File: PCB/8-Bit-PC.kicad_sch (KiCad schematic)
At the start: 0 parts

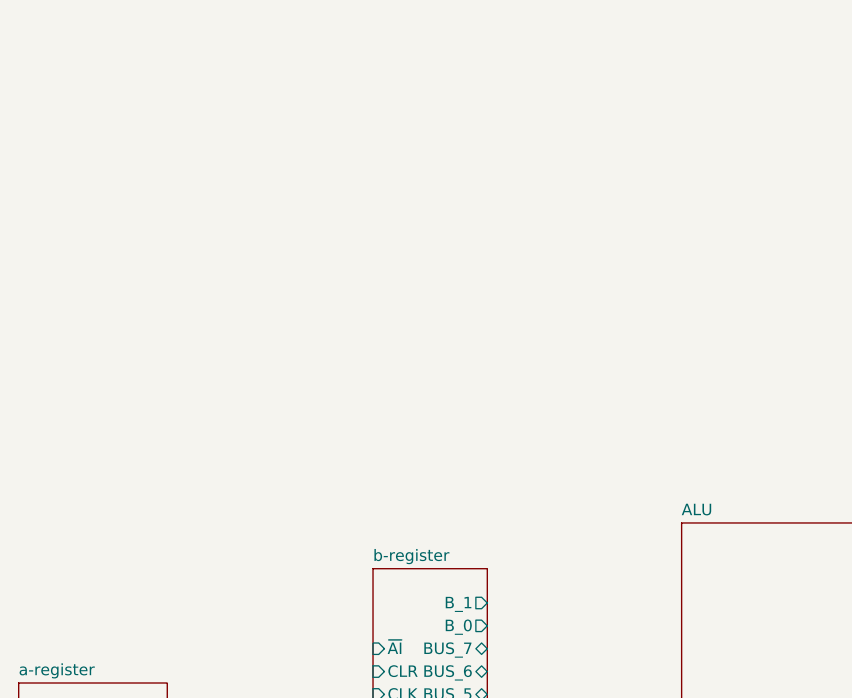
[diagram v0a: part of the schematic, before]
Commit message: got ready to add the cpu control and and out put modules
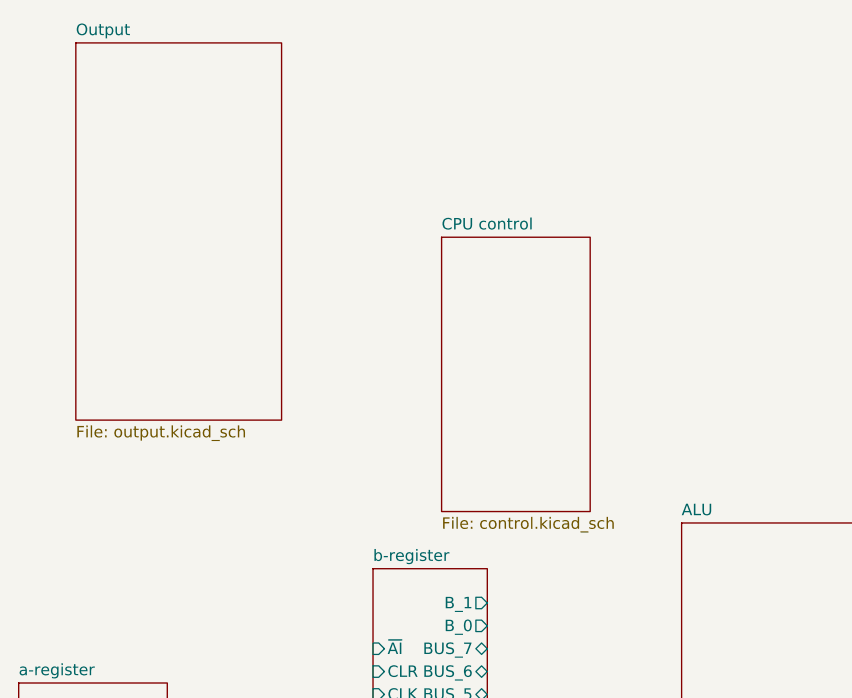
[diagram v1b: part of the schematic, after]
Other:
- added sheet CPU control (control.kicad_sch)
- added sheet Output (output.kicad_sch)
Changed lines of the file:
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@@
+	)
+	(sheet
+		(at 29.21 36.83)
+		(size 22.86 41.91)
+		(exclude_from_sim no)
+		(in_bom yes)
+		(on_board yes)
+		(dnp no)
+		(fields_autoplaced yes)
+		(stroke
+			(width 0.1524)
+			(type solid)
+		)
+		(fill
+			(color 0 0 0 0.0000)
+		)
+		(property "Sheetname" "Output"
+			(at 29.21 36.1184 0)
+			(effects
+				(font
+					(size 1.27 1.27)
+				)
+				(justify left bottom)
+			)
+		)
+		(property "Sheetfile" "output.kicad_sch"
+			(at 29.21 79.3246 0)
+			(effects
+				(font
+					(size 1.27 1.27)
+				)
+				(justify left top)
+			)
+		)
+		(instances
+			(project "8-Bit-PC"
+				(path "/48633dea-2de9-4b6f-aeff-2ee54233f918"
+					(page "9")
+				)
+			)
+		)
+	)
+	(sheet
+		(at 69.85 58.42)
+		(size 16.51 30.48)
+		(exclude_from_sim no)
+		(in_bom yes)
+		(on_board yes)
+		(dnp no)
+		(fields_autoplaced yes)
+		(stroke
+			(width 0.1524)
+			(type solid)
+		)
+		(fill
+			(color 0 0 0 0.0000)
+		)
+		(property "Sheetname" "CPU control"
+			(at 69.85 57.7084 0)
+			(effects
+				(font
+					(size 1.27 1.27)
+				)
+				(justify left bottom)
+			)
+		)
+		(property "Sheetfile" "control.kicad_sch"
+			(at 69.85 89.4846 0)
+			(effects
+				(font
+					(size 1.27 1.27)
+				)
+				(justify left top)
+			)
+		)
+		(instances
+			(project "8-Bit-PC"
+				(path "/48633dea-2de9-4b6f-aeff-2ee54233f918"
+					(page "10")
+				)
+			)
+		)
 	)
 	(sheet

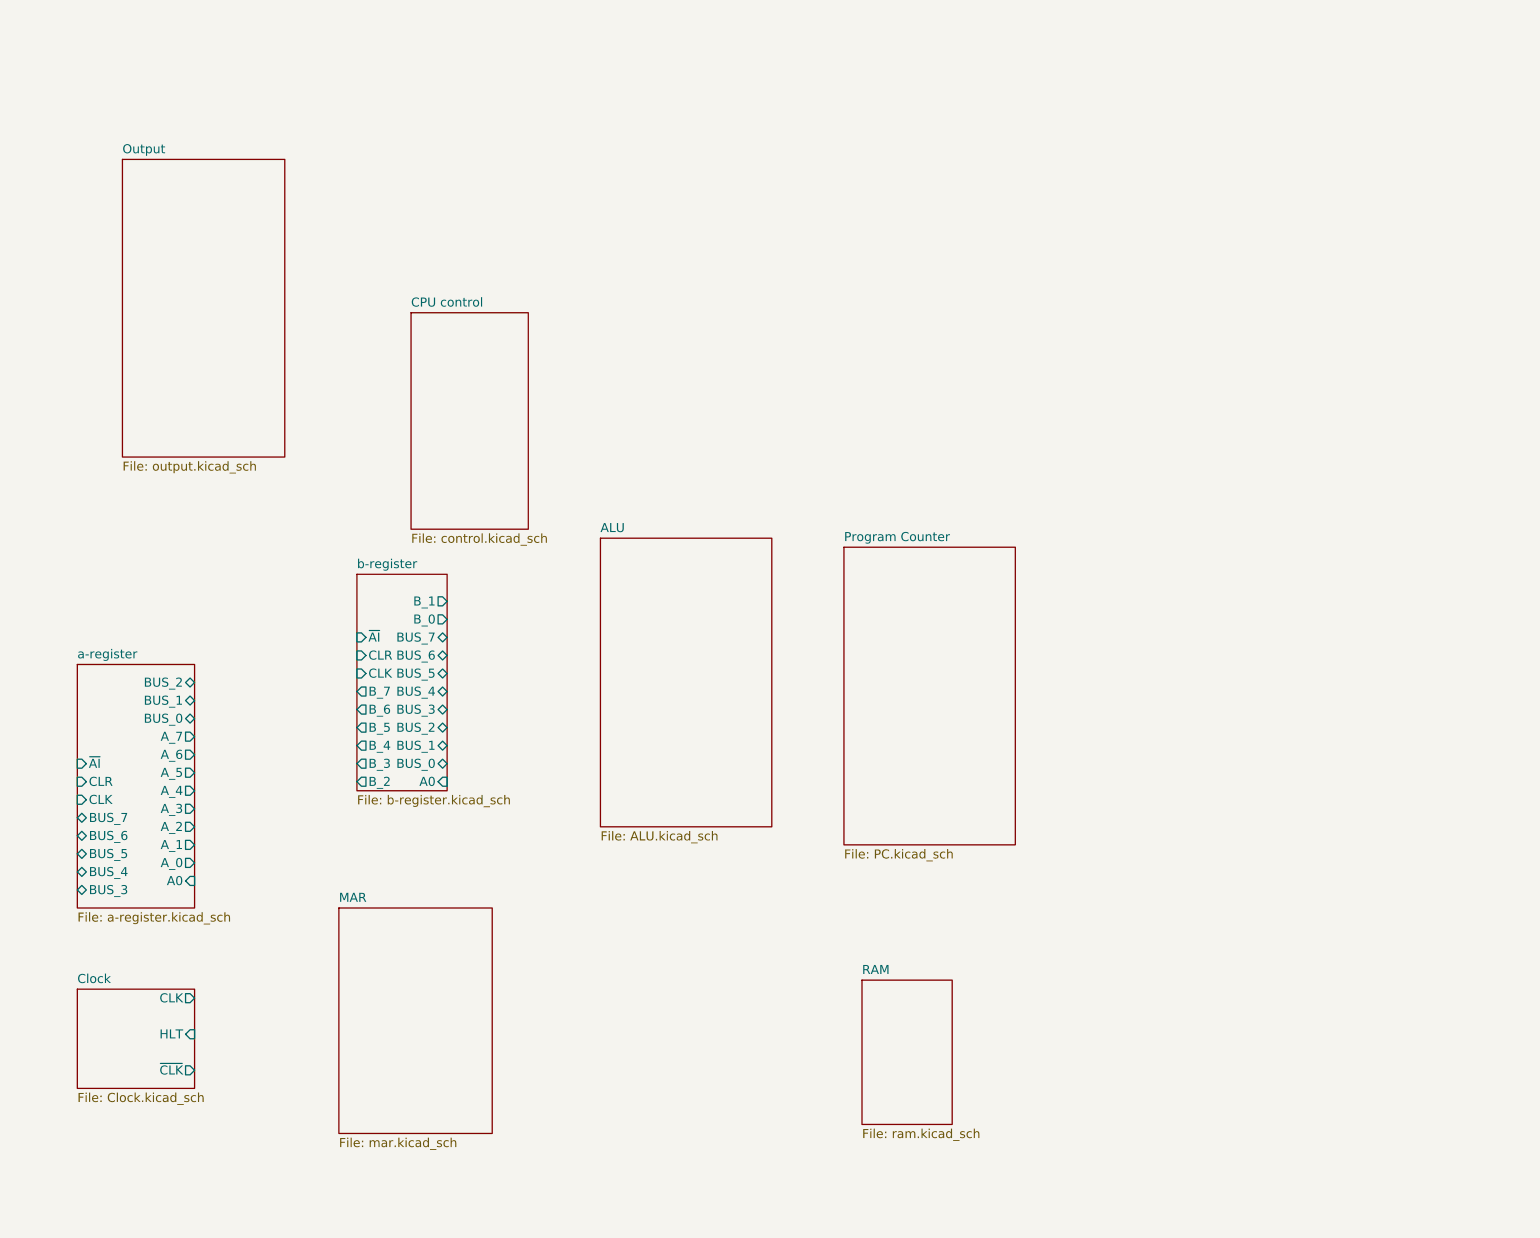
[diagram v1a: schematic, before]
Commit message: Cleaned up the schematic and got started on assigning all the footprints to the symbols
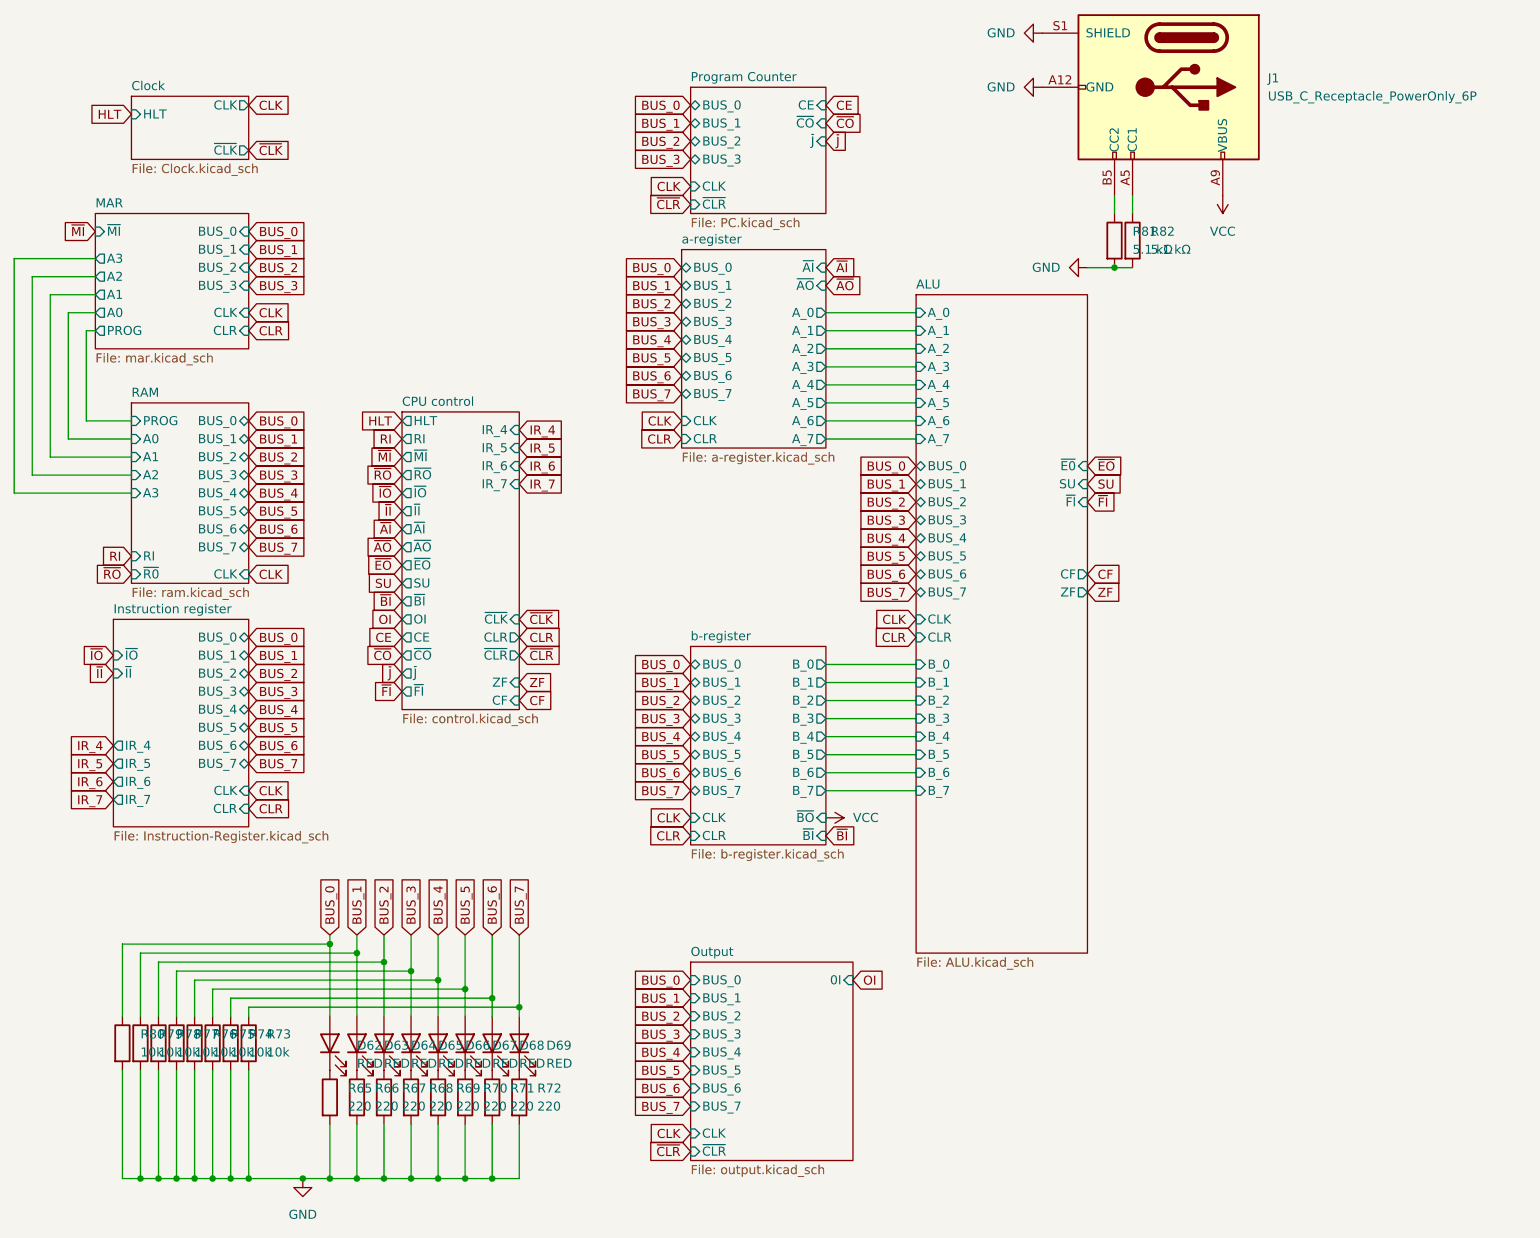
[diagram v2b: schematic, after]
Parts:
- added D62, D63, D64, D65, D66, D67, D68, D69: RED, LED_THT:LED_D1.8mm_W1.8mm_H2.4mm_Horizontal_O1.27mm_Z1.6mm, symbol Device:LED
- added J1: USB_C_Receptacle_PowerOnly_6P, Connector_USB:USB_C_Receptacle_HRO_TYPE-C-31-M-17, symbol Connector:USB_C_Receptacle_PowerOnly_6P
- added R65, R66, R67, R68, R69, R70, R71, R72: 220, Resistor_THT:R_Axial_DIN0207_L6.3mm_D2.5mm_P7.62mm_Horizontal, symbol Device:R
- added R73, R74, R75, R76, R77, R78, R79, R80: 10k, Resistor_THT:R_Axial_DIN0207_L6.3mm_D2.5mm_P7.62mm_Horizontal, symbol Device:R
- added R81, R82: 5.1 kΩ, Resistor_THT:R_Axial_DIN0207_L6.3mm_D2.5mm_P7.62mm_Horizontal, symbol Device:R
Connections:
- new net: D64.1 (K), R67.1
- new net: D69.1 (K), R72.1
- new net: D68.1 (K), R71.1
- new net: D65.1 (K), R68.1
- new net: J1.A5 (CC1), R82.1
- new net: J1.B5 (CC2), R81.1
- new net: D63.1 (K), R66.1
- new net: D62.1 (K), R65.1
- new net: D67.1 (K), R70.1
- new net: D66.1 (K), R69.1
- new net BUS_0: D62.2 (A), R80.1
- new net BUS_1: D63.2 (A), R79.1
- new net BUS_2: D64.2 (A), R78.1
- new net BUS_3: D65.2 (A), R77.1
- new net BUS_4: D66.2 (A), R76.1
- new net BUS_5: D67.2 (A), R75.1
- new net BUS_6: D68.2 (A), R74.1
- new net BUS_7: D69.2 (A), R73.1
- new net GND: J1.A12 (GND), J1.B12 (GND), J1.S1 (SHIELD), R65.2, R66.2, R67.2, R68.2, R69.2, R70.2, R71.2, R72.2, R73.2, R74.2, R75.2, R76.2, R77.2, R78.2, R79.2, R80.2, R81.2, R82.2
- new net VCC: J1.A9 (VBUS), J1.B9 (VBUS)
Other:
- added sheet Instruction register (Instruction-Register.kicad_sch)
- sheet ALU ports: added A_0, A_1, A_2, A_3, A_4, A_5, A_6, A_7, BUS_0, BUS_1, BUS_2, BUS_3, BUS_4, BUS_5, BUS_6, BUS_7, B_0, B_1, B_2, B_3, B_4, B_5, B_6, B_7, CF, CLK, CLR, SU, ZF, ~{E0}, ~{Fl}; removed none
- sheet CPU control ports: added CE, CF, CLR, HLT, IR_4, IR_5, IR_6, IR_7, OI, RI, SU, ZF, ~{AI}, ~{AO}, ~{BI}, ~{CLK}, ~{CLR}, ~{CO}, ~{EO}, ~{FI}, ~{II}, ~{IO}, ~{J}, ~{MI}, ~{RO}; removed none
- sheet MAR ports: added A0, A1, A2, A3, BUS_0, BUS_1, BUS_2, BUS_3, CLK, CLR, PROG, ~{MI}; removed none
- sheet Output ports: added 0I, BUS_0, BUS_1, BUS_2, BUS_3, BUS_4, BUS_5, BUS_6, BUS_7, CLK, ~{CLR}; removed none
- sheet Program Counter ports: added BUS_0, BUS_1, BUS_2, BUS_3, CE, CLK, ~{CLR}, ~{CO}, ~{J}; removed none
- sheet RAM ports: added A0, A1, A2, A3, BUS_0, BUS_1, BUS_2, BUS_3, BUS_4, BUS_5, BUS_6, BUS_7, CLK, PROG, RI, ~{R0}; removed none
- sheet a-register ports: added ~{AO}; removed A0
- sheet b-register ports: added ~{BI}, ~{BO}; removed A0, ~{AI}

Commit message: added more models to work with on my pcb
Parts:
- D62, D63, D64, D65, D66, D67, D68, D69: footprint LED_THT:LED_D1.8mm_W1.8mm_H2.4mm_Horizontal_O1.27mm_Z1.6mm -> LED_THT:LED_D3.0mm
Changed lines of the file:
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@@
 			)
 		)
-		(property "Footprint" "LED_THT:LED_D1.8mm_W1.8mm_H2.4mm_Horizontal_O1.27mm_Z1.6mm"
+		(property "Footprint" "LED_THT:LED_D3.0mm"
 			(at 85.09 161.29 0)
 			(effects
@@
 			)
 		)
-		(property "Footprint" "LED_THT:LED_D1.8mm_W1.8mm_H2.4mm_Horizontal_O1.27mm_Z1.6mm"
+		(property "Footprint" "LED_THT:LED_D3.0mm"
 			(at 81.28 161.29 0)
 			(effects
@@
 			)
 		)
-		(property "Footprint" "LED_THT:LED_D1.8mm_W1.8mm_H2.4mm_Horizontal_O1.27mm_Z1.6mm"
+		(property "Footprint" "LED_THT:LED_D3.0mm"
 			(at 62.23 161.29 0)
 			(effects
@@
 			)
 		)
-		(property "Footprint" "LED_THT:LED_D1.8mm_W1.8mm_H2.4mm_Horizontal_O1.27mm_Z1.6mm"
+		(property "Footprint" "LED_THT:LED_D3.0mm"
 			(at 73.66 161.29 0)
 			(effects
@@
 			)
 		)
-		(property "Footprint" "LED_THT:LED_D1.8mm_W1.8mm_H2.4mm_Horizontal_O1.27mm_Z1.6mm"
+		(property "Footprint" "LED_THT:LED_D3.0mm"
 			(at 58.42 161.29 0)
 			(effects
@@
 			)
 		)
-		(property "Footprint" "LED_THT:LED_D1.8mm_W1.8mm_H2.4mm_Horizontal_O1.27mm_Z1.6mm"
+		(property "Footprint" "LED_THT:LED_D3.0mm"
 			(at 77.47 161.29 0)
 			(effects
@@
 			)
 		)
-		(property "Footprint" "LED_THT:LED_D1.8mm_W1.8mm_H2.4mm_Horizontal_O1.27mm_Z1.6mm"
+		(property "Footprint" "LED_THT:LED_D3.0mm"
 			(at 66.04 161.29 0)
 			(effects
@@
 			)
 		)
-		(property "Footprint" "LED_THT:LED_D1.8mm_W1.8mm_H2.4mm_Horizontal_O1.27mm_Z1.6mm"
+		(property "Footprint" "LED_THT:LED_D3.0mm"
 			(at 69.85 161.29 0)
 			(effects

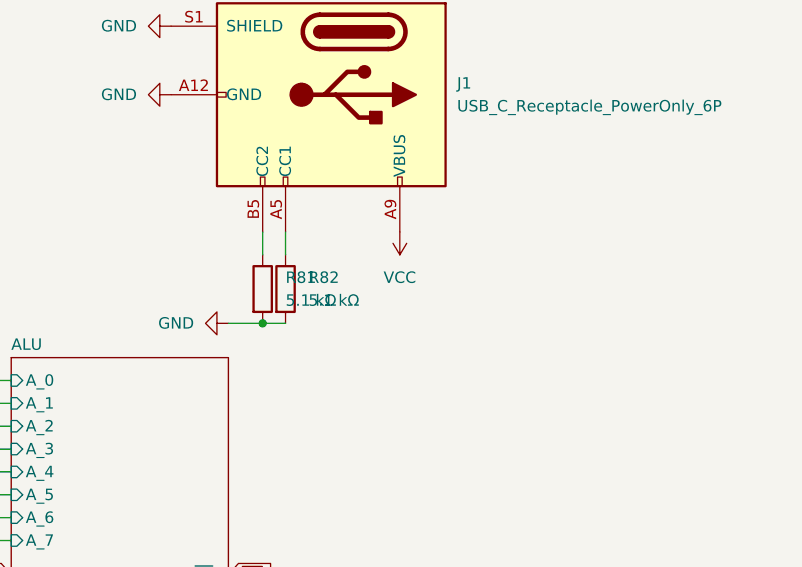
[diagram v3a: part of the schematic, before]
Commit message: Add decupling caps and reroute pcb. Updated BOM to match new number of caps
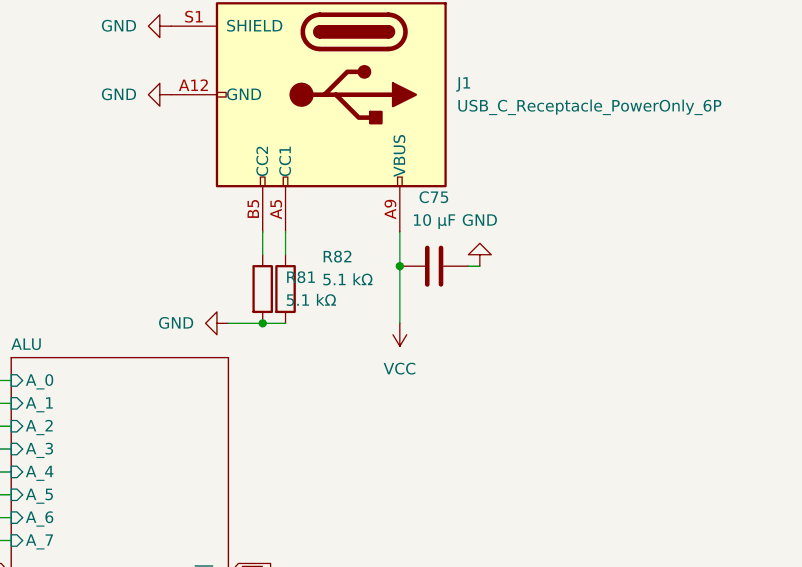
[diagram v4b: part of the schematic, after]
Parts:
- added C75: 10 µF, Capacitor_THT:C_Radial_D5.0mm_H5.0mm_P2.00mm, symbol Device:C
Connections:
- net GND: now also C75.2
- net VCC: now also C75.1
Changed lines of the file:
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@@
 	)
 	(junction
+		(at 184.15 45.72)
+		(diameter 0)
+		(color 0 0 0 0)
+	)
+	(junction
 		(at 62.23 180.34)
 		(diameter 0)
@@
 	(wire
 		(pts
+			(xy 191.77 45.72) (xy 193.04 45.72)
+		)
+		(stroke
+			(width 0)
+			(type default)
+		)
+	)
+	(wire
+		(pts
 			(xy 128.27 113.03) (xy 140.97 113.03)
 		)
@@
 	(wire
 		(pts
+			(xy 184.15 45.72) (xy 184.15 52.07)
+		)
+		(stroke
+			(width 0)
+			(type default)
+		)
+	)
+	(wire
+		(pts
 			(xy 21.59 76.2) (xy 30.48 76.2)
 		)
@@
 	(wire
 		(pts
+			(xy 184.15 41.91) (xy 184.15 45.72)
+		)
+		(stroke
+			(width 0)
+			(type default)
+		)
+	)
+	(wire
+		(pts
 			(xy 25.4 50.8) (xy 13.97 50.8)
 		)
@@
 	(symbol
 		(lib_id "power:GND")
+		(at 193.04 45.72 180)
+		(unit 1)
+		(exclude_from_sim no)
+		(in_bom yes)
+		(on_board yes)
+		(dnp no)
+		(fields_autoplaced yes)
+		(property "Reference" "#PWR0220"
+			(at 193.04 39.37 0)
+			(effects
+				(font
+					(size 1.27 1.27)
+				)
+				(hide yes)
+			)
+		)
+		(property "Value" "GND"
+			(at 193.04 40.64 0)
+			(effects
+				(font
+					(size 1.27 1.27)
+				)
+			)
+		)
+		(property "Footprint" ""
+			(at 193.04 45.72 0)
+			(effects
+				(font
+					(size 1.27 1.27)
+				)
+				(hide yes)
+			)
+		)
+		(property "Datasheet" ""
+			(at 193.04 45.72 0)
+			(effects
+				(font
+					(size 1.27 1.27)
+				)
+				(hide yes)
+			)
+		)
+		(property "Description" "Power symbol creates a global label with name \"GND\" , ground"
+			(at 193.04 45.72 0)
+			(effects
+				(font
+					(size 1.27 1.27)
+				)
+				(hide yes)
+			)
+		)
+		(pin "1"
+		)
+		(instances
+			(project "8-Bit-PC"
+				(path "/48633dea-2de9-4b6f-aeff-2ee54233f918"
+					(reference "#PWR0220")
+					(unit 1)
+				)
+			)
+		)
+	)
+	(symbol
+		(lib_id "power:GND")
 		(at 165.1 52.07 270)
 		(unit 1)
@@
 	(symbol
 		(lib_id "power:VCC")
-		(at 184.15 41.91 180)
+		(at 184.15 52.07 180)
 		(unit 1)
 		(exclude_from_sim no)
@@
 		(fields_autoplaced yes)
 		(property "Reference" "#PWR0104"
-			(at 184.15 38.1 0)
+			(at 184.15 48.26 0)
 			(effects
 				(font
@@
 		)
 		(property "Value" "VCC"
-			(at 184.15 46.99 0)
+			(at 184.15 57.15 0)
 			(effects
 				(font
@@
 		)
 		(property "Footprint" ""
-			(at 184.15 41.91 0)
+			(at 184.15 52.07 0)
 			(effects
 				(font
@@
 		)
 		(property "Datasheet" ""
-			(at 184.15 41.91 0)
+			(at 184.15 52.07 0)
 			(effects
 				(font
@@
 		)
 		(property "Description" "Power symbol creates a global label with name \"VCC\""
-			(at 184.15 41.91 0)
+			(at 184.15 52.07 0)
 			(effects
 				(font
@@
 	)
 	(symbol
+		(lib_id "Device:C")
+		(at 187.96 45.72 90)
+		(unit 1)
+		(exclude_from_sim no)
+		(in_bom yes)
+		(on_board yes)
+		(dnp no)
+		(fields_autoplaced yes)
+		(property "Reference" "C75"
+			(at 187.96 38.1 90)
+			(effects
+				(font
+					(size 1.27 1.27)
+				)
+			)
+		)
+		(property "Value" "10 µF"
+			(at 187.96 40.64 90)
+			(effects
+				(font
+					(size 1.27 1.27)
+				)
+			)
+		)
+		(property "Footprint" "Capacitor_THT:C_Radial_D5.0mm_H5.0mm_P2.00mm"
+			(at 191.77 44.7548 0)
+			(effects
+				(font
+					(size 1.27 1.27)
+				)
+				(hide yes)
+			)
+		)
+		(property "Datasheet" "~"
+			(at 187.96 45.72 0)
+			(effects
+				(font
+					(size 1.27 1.27)
+				)
+				(hide yes)
+			)
+		)
+		(property "Description" "Unpolarized capacitor"
+			(at 187.96 45.72 0)
+			(effects
+				(font
+					(size 1.27 1.27)
+				)
+				(hide yes)
+			)
+		)
+		(pin "1"
+		)
+		(pin "2"
+		)
+		(instances
+			(project "8-Bit-PC"
+				(path "/48633dea-2de9-4b6f-aeff-2ee54233f918"
+					(reference "C75")
+					(unit 1)
+				)
+			)
+		)
+	)
+	(symbol
 		(lib_id "Device:R")
 		(at 44.45 161.29 0)
@@
 		(on_board yes)
 		(dnp no)
-		(fields_autoplaced yes)
 		(property "Reference" "R82"
-			(at 173.99 46.9899 0)
+			(at 175.514 44.704 0)
 			(effects
 				(font
@@
 		)
 		(property "Value" "5.1 kΩ"
-			(at 173.99 49.5299 0)
+			(at 175.514 47.244 0)
 			(effects
 				(font
